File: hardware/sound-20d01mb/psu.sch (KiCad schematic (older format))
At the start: 3 parts

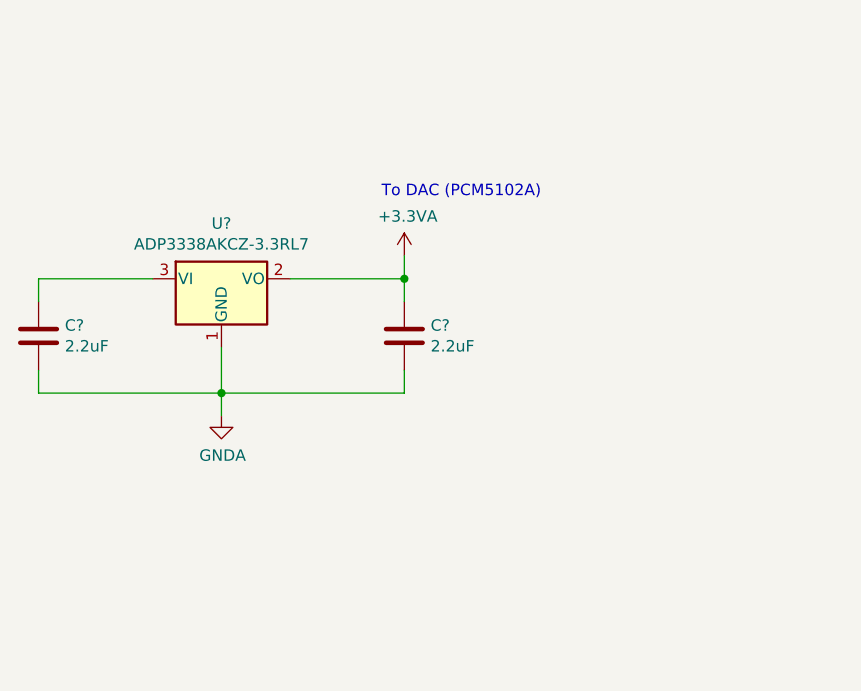
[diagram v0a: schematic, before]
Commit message: Updated power supply unit
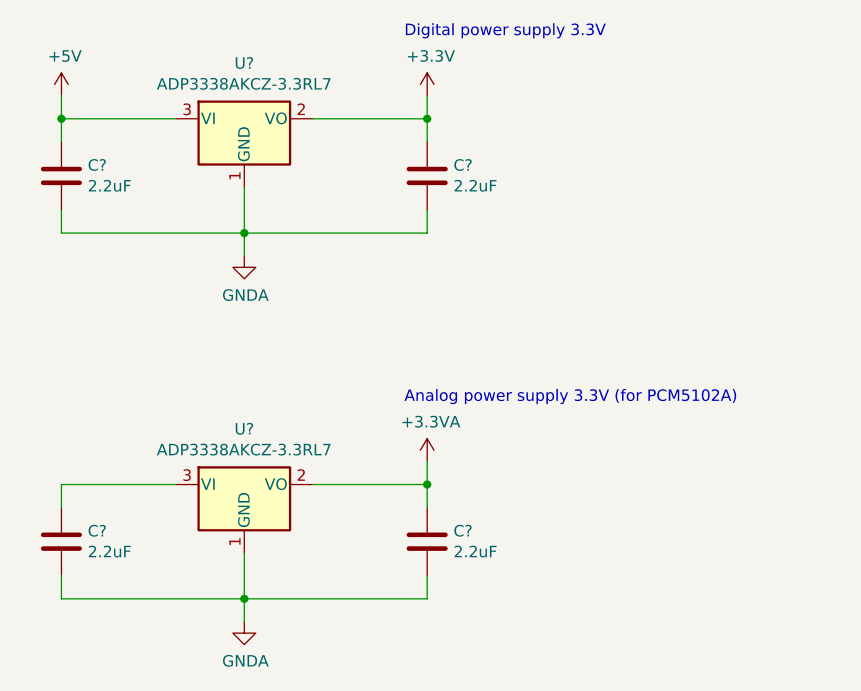
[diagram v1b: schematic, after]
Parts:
- added C? (x2): 2.2uF, Capacitor_SMD:C_1206_3216Metric_Pad1.42x1.75mm_HandSolder, symbol Device:C
- added U?: ADP3338AKCZ-3.3RL7, Package_TO_SOT_SMD:SOT-223-3_TabPin2, symbol Regulator_Linear:AZ1117-3.3
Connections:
- net GNDA: now also C?.2, C?.2, U?.1 (GND)
- new net +3V3: C?.1, U?.2 (VO)
- new net +5V: C?.1, U?.3 (VI)
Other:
- note added: "Analog power supply 3.3V (for PCM5102A)"
- note added: "Digital power supply 3.3V"
- note removed: "To DAC (PCM5102A)"
- moved on the sheet: C?, U?
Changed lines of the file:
@@
 L Regulator_Linear:AZ1117-3.3 U?
 U 1 1 60DF628F
-P 4350 3150
-F 0 "U?" H 4350 3392 50  0000 C CNN
-F 1 "ADP3338AKCZ-3.3RL7" H 4350 3301 50  0000 C CNN
-F 2 "Package_TO_SOT_SMD:SOT-223-3_TabPin2" H 4350 3400 50  0001 C CIN
-F 3 "https://www.analog.com/media/en/technical-documentation/data-sheets/adp3338.pdf" H 4350 3150 50  0001 C CNN
-	1    4350 3150
+P 4450 4050
+F 0 "U?" H 4450 4292 50  0000 C CNN
+F 1 "ADP3338AKCZ-3.3RL7" H 4450 4201 50  0000 C CNN
+F 2 "Package_TO_SOT_SMD:SOT-223-3_TabPin2" H 4450 4300 50  0001 C CIN
+F 3 "https://www.analog.com/media/en/technical-documentation/data-sheets/adp3338.pdf" H 4450 4050 50  0001 C CNN
+	1    4450 4050
 	1    0    0    -1
 $EndComp
@@
 L Device:C C?
 U 1 1 60E015B2
-P 5150 3400
+P 5250 4300
 AR Path="/60DE2DF4/60E015B2" Ref="C?"  Part="1"
 AR Path="/60DE2DF1/60E015B2" Ref="C?"  Part="1"
 AR Path="/61033008/60E015B2" Ref="C?"  Part="1"
-F 0 "C?" H 5265 3446 50  0000 L CNN
-F 1 "2.2uF" H 5265 3355 50  0000 L CNN
-F 2 "Capacitor_SMD:C_1206_3216Metric_Pad1.42x1.75mm_HandSolder" H 5188 3250 50  0001 C CNN
-F 3 "~" H 5150 3400 50  0001 C CNN
-	1    5150 3400
+F 0 "C?" H 5365 4346 50  0000 L CNN
+F 1 "2.2uF" H 5365 4255 50  0000 L CNN
+F 2 "Capacitor_SMD:C_1206_3216Metric_Pad1.42x1.75mm_HandSolder" H 5288 4150 50  0001 C CNN
+F 3 "~" H 5250 4300 50  0001 C CNN
+	1    5250 4300
 	1    0    0    -1
 $EndComp
@@
 L Device:C C?
 U 1 1 60E01602
-P 3550 3400
+P 3650 4300
 AR Path="/60DE2DF4/60E01602" Ref="C?"  Part="1"
 AR Path="/60DE2DF1/60E01602" Ref="C?"  Part="1"
 AR Path="/61033008/60E01602" Ref="C?"  Part="1"
-F 0 "C?" H 3665 3446 50  0000 L CNN
-F 1 "2.2uF" H 3665 3355 50  0000 L CNN
-F 2 "Capacitor_SMD:C_1206_3216Metric_Pad1.42x1.75mm_HandSolder" H 3588 3250 50  0001 C CNN
-F 3 "~" H 3550 3400 50  0001 C CNN
-	1    3550 3400
+F 0 "C?" H 3765 4346 50  0000 L CNN
+F 1 "2.2uF" H 3765 4255 50  0000 L CNN
+F 2 "Capacitor_SMD:C_1206_3216Metric_Pad1.42x1.75mm_HandSolder" H 3688 4150 50  0001 C CNN
+F 3 "~" H 3650 4300 50  0001 C CNN
+	1    3650 4300
 	1    0    0    -1
 $EndComp
@@
 L power:GNDA #PWR?
 U 1 1 60E01644
-P 4350 3750
-F 0 "#PWR?" H 4350 3500 50  0001 C CNN
-F 1 "GNDA" H 4355 3577 50  0000 C CNN
-F 2 "" H 4350 3750 50  0001 C CNN
-F 3 "" H 4350 3750 50  0001 C CNN
-	1    4350 3750
+P 4450 4650
+F 0 "#PWR?" H 4450 4400 50  0001 C CNN
+F 1 "GNDA" H 4455 4477 50  0000 C CNN
+F 2 "" H 4450 4650 50  0001 C CNN
+F 3 "" H 4450 4650 50  0001 C CNN
+	1    4450 4650
 	1    0    0    -1
 $EndComp
 Wire Wire Line
-	4350 3450 4350 3650
+	4450 4350 4450 4550
 $Comp
 L power:+3.3VA #PWR?
 U 1 1 60E017A8
-P 5150 3050
-F 0 "#PWR?" H 5150 2900 50  0001 C CNN
-F 1 "+3.3VA" H 5165 3223 50  0000 C CNN
-F 2 "" H 5150 3050 50  0001 C CNN
-F 3 "" H 5150 3050 50  0001 C CNN
-	1    5150 3050
+P 5250 3950
+F 0 "#PWR?" H 5250 3800 50  0001 C CNN
+F 1 "+3.3VA" H 5265 4123 50  0000 C CNN
+F 2 "" H 5250 3950 50  0001 C CNN
+F 3 "" H 5250 3950 50  0001 C CNN
+	1    5250 3950
 	1    0    0    -1
 $EndComp
 Wire Wire Line
-	4650 3150 5150 3150
+	4750 4050 5250 4050
 Wire Wire Line
-	5150 3150 5150 3050
+	5250 4050 5250 3950
 Wire Wire Line
-	5150 3150 5150 3250
-Connection ~ 5150 3150
+	5250 4050 5250 4150
+Connection ~ 5250 4050
 Wire Wire Line
-	5150 3550 5150 3650
+	5250 4450 5250 4550
 Wire Wire Line
-	5150 3650 4350 3650
+	5250 4550 4450 4550
 Wire Wire Line
-	4350 3650 4350 3750
-Connection ~ 4350 3650
+	4450 4550 4450 4650
+Connection ~ 4450 4550
 Wire Wire Line
-	3550 3150 4050 3150
+	3650 4050 4150 4050
 Wire Wire Line
-	4350 3650 3550 3650
+	4450 4550 3650 4550
 Wire Wire Line
-	3550 3650 3550 3550
+	3650 4550 3650 4450
 Wire Wire Line
-	3550 3150 3550 3250
-Text Notes 5050 2800 0    50   ~ 0
-To DAC (PCM5102A)
+	3650 4050 3650 4150
+Text Notes 5150 3700 0    50   ~ 0
+Analog power supply 3.3V (for PCM5102A)
+$Comp
+L Regulator_Linear:AZ1117-3.3 U?
+U 1 1 60E0E9BB
+P 4450 2450
+F 0 "U?" H 4450 2692 50  0000 C CNN
+F 1 "ADP3338AKCZ-3.3RL7" H 4450 2601 50  0000 C CNN
+F 2 "Package_TO_SOT_SMD:SOT-223-3_TabPin2" H 4450 2700 50  0001 C CIN
+F 3 "https://www.analog.com/media/en/technical-documentation/data-sheets/adp3338.pdf" H 4450 2450 50  0001 C CNN
+	1    4450 2450
+	1    0    0    -1
+$EndComp
+$Comp
+L Device:C C?
+U 1 1 60E0E9C1
+P 5250 2700
+AR Path="/60DE2DF4/60E0E9C1" Ref="C?"  Part="1"
+AR Path="/60DE2DF1/60E0E9C1" Ref="C?"  Part="1"
+AR Path="/61033008/60E0E9C1" Ref="C?"  Part="1"
+F 0 "C?" H 5365 2746 50  0000 L CNN
+F 1 "2.2uF" H 5365 2655 50  0000 L CNN
+F 2 "Capacitor_SMD:C_1206_3216Metric_Pad1.42x1.75mm_HandSolder" H 5288 2550 50  0001 C CNN
+F 3 "~" H 5250 2700 50  0001 C CNN
+	1    5250 2700
+	1    0    0    -1
+$EndComp
+$Comp
+L Device:C C?
+U 1 1 60E0E9C7
+P 3650 2700
+AR Path="/60DE2DF4/60E0E9C7" Ref="C?"  Part="1"
+AR Path="/60DE2DF1/60E0E9C7" Ref="C?"  Part="1"
+AR Path="/61033008/60E0E9C7" Ref="C?"  Part="1"
+F 0 "C?" H 3765 2746 50  0000 L CNN
+F 1 "2.2uF" H 3765 2655 50  0000 L CNN
+F 2 "Capacitor_SMD:C_1206_3216Metric_Pad1.42x1.75mm_HandSolder" H 3688 2550 50  0001 C CNN
+F 3 "~" H 3650 2700 50  0001 C CNN
+	1    3650 2700
+	1    0    0    -1
+$EndComp
+$Comp
+L power:GNDA #PWR?
+U 1 1 60E0E9CD
+P 4450 3050
+F 0 "#PWR?" H 4450 2800 50  0001 C CNN
+F 1 "GNDA" H 4455 2877 50  0000 C CNN
+F 2 "" H 4450 3050 50  0001 C CNN
+F 3 "" H 4450 3050 50  0001 C CNN
+	1    4450 3050
+	1    0    0    -1
+$EndComp
+Wire Wire Line
+	4450 2750 4450 2950
+Wire Wire Line
+	4750 2450 5250 2450
+Wire Wire Line
+	5250 2450 5250 2350
+Wire Wire Line
+	5250 2450 5250 2550
+Connection ~ 5250 2450
+Wire Wire Line
+	5250 2850 5250 2950
+Wire Wire Line
+	5250 2950 4450 2950
+Wire Wire Line
+	4450 2950 4450 3050
+Connection ~ 4450 2950
+Wire Wire Line
+	3650 2450 4150 2450
+Wire Wire Line
+	4450 2950 3650 2950
+Wire Wire Line
+	3650 2950 3650 2850
+Wire Wire Line
+	3650 2450 3650 2550
+$Comp
+L power:+3.3V #PWR?
+U 1 1 60E0F338
+P 5250 2350
+F 0 "#PWR?" H 5250 2200 50  0001 C CNN
+F 1 "+3.3V" H 5265 2523 50  0000 C CNN
+F 2 "" H 5250 2350 50  0001 C CNN
+F 3 "" H 5250 2350 50  0001 C CNN
+	1    5250 2350
+	1    0    0    -1
+$EndComp
+$Comp
+L power:+5V #PWR?
+U 1 1 60E0F3AB
+P 3650 2350
+F 0 "#PWR?" H 3650 2200 50  0001 C CNN
+F 1 "+5V" H 3665 2523 50  0000 C CNN
+F 2 "" H 3650 2350 50  0001 C CNN
+F 3 "" H 3650 2350 50  0001 C CNN
+	1    3650 2350
+	1    0    0    -1
+$EndComp
+Wire Wire Line
+	3650 2350 3650 2450
+Connection ~ 3650 2450
+Text Notes 5150 2100 0    50   ~ 0
+Digital power supply 3.3V
 $EndSCHEMATC

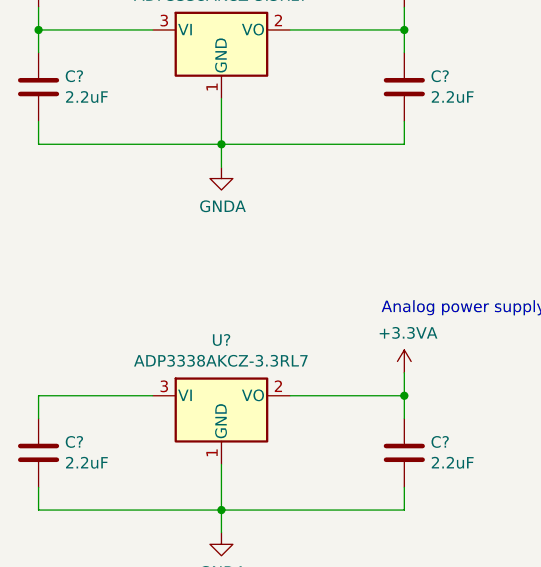
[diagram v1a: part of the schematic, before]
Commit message: Added Gain Settings
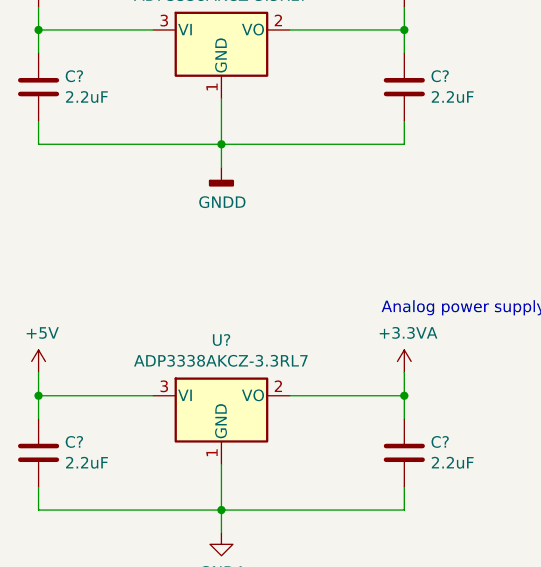
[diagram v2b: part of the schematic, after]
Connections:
- net +5V: now also C?.1, U?.3 (VI)
- net GNDA: no longer C?.2, C?.2, U?.1 (GND)
- new net GNDD: C?.2, C?.2, U?.1 (GND)
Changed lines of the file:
@@
-	1    0    0    -1
-$EndComp
-$Comp
-L power:GNDA #PWR?
-U 1 1 60E0E9CD
-P 4450 3050
-F 0 "#PWR?" H 4450 2800 50  0001 C CNN
-F 1 "GNDA" H 4455 2877 50  0000 C CNN
-F 2 "" H 4450 3050 50  0001 C CNN
-F 3 "" H 4450 3050 50  0001 C CNN
-	1    4450 3050
 	1    0    0    -1
 $EndComp
@@
 Text Notes 5150 2100 0    50   ~ 0
 Digital power supply 3.3V
+$Comp
+L power:GNDD #PWR?
+U 1 1 60E17887
+P 4450 3050
+F 0 "#PWR?" H 4450 2800 50  0001 C CNN
+F 1 "GNDD" H 4454 2895 50  0000 C CNN
+F 2 "" H 4450 3050 50  0001 C CNN
+F 3 "" H 4450 3050 50  0001 C CNN
+	1    4450 3050
+	1    0    0    -1
+$EndComp
+$Comp
+L power:+5V #PWR?
+U 1 1 60E17DB7
+P 3650 3950
+F 0 "#PWR?" H 3650 3800 50  0001 C CNN
+F 1 "+5V" H 3665 4123 50  0000 C CNN
+F 2 "" H 3650 3950 50  0001 C CNN
+F 3 "" H 3650 3950 50  0001 C CNN
+	1    3650 3950
+	1    0    0    -1
+$EndComp
+Wire Wire Line
+	3650 3950 3650 4050
+Connection ~ 3650 4050
 $EndSCHEMATC

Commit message: Updated PSU
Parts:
- added C?: 47uF, symbol Device:CP
- added C? (x2): 10uF, symbol Device:CP
- added C? (x2): 470uF, symbol Device:CP
- added C? (x2): 0.1uF, Capacitor_SMD:C_1206_3216Metric_Pad1.42x1.75mm_HandSolder, symbol Device:C
- added JP?: Jumper_3_Bridged12, Connector_PinHeader_2.54mm:PinHeader_1x03_P2.54mm_Vertical, symbol Jumper:Jumper_3_Bridged12
- added U?: L7805, symbol Regulator_Linear:L7805
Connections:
- net +3V3: now also C?.1
- net +5V: now also C?.1, C?.1, JP?.2 (C); no longer C?.1, U?.3 (VI)
- net GNDA: now also C?.2, C?.2, C?.2, C?.2, U?.2 (GND)
- net GNDD: now also C?.2, C?.2, C?.2
- new net: C?.1, C?.1, C?.1, U?.3 (OUT), U?.3 (VI)
- new net EXT_5V: JP?.3 (B)
- new net VBUS: JP?.1 (A)
- new net VCC: C?.1, C?.1, U?.1 (IN)
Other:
- note added: "Analog power supply +3.3VA (PCM5102A)"
- note added: "Digital power supply +3.3V"
- note added: "Place U? as close to the MCU as possible."
- note removed: "Analog power supply 3.3V (for PCM5102A)"
- note removed: "Digital power supply 3.3V"
- moved on the sheet: C?, U?

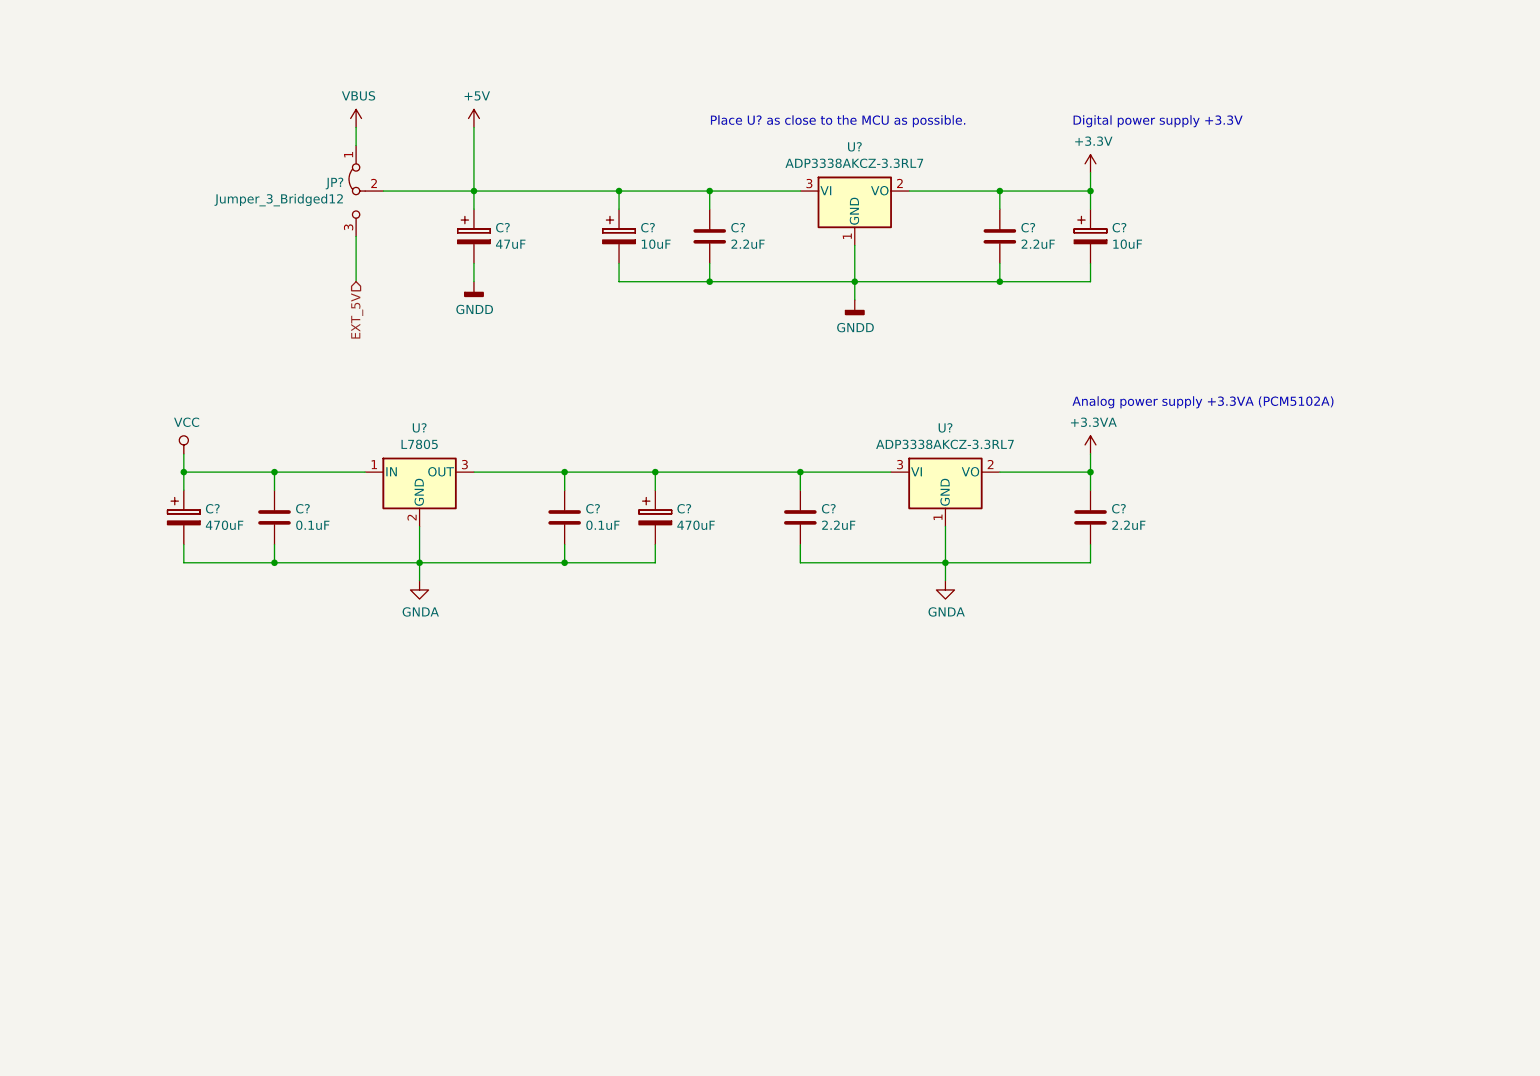
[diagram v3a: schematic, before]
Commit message: Added LM27762
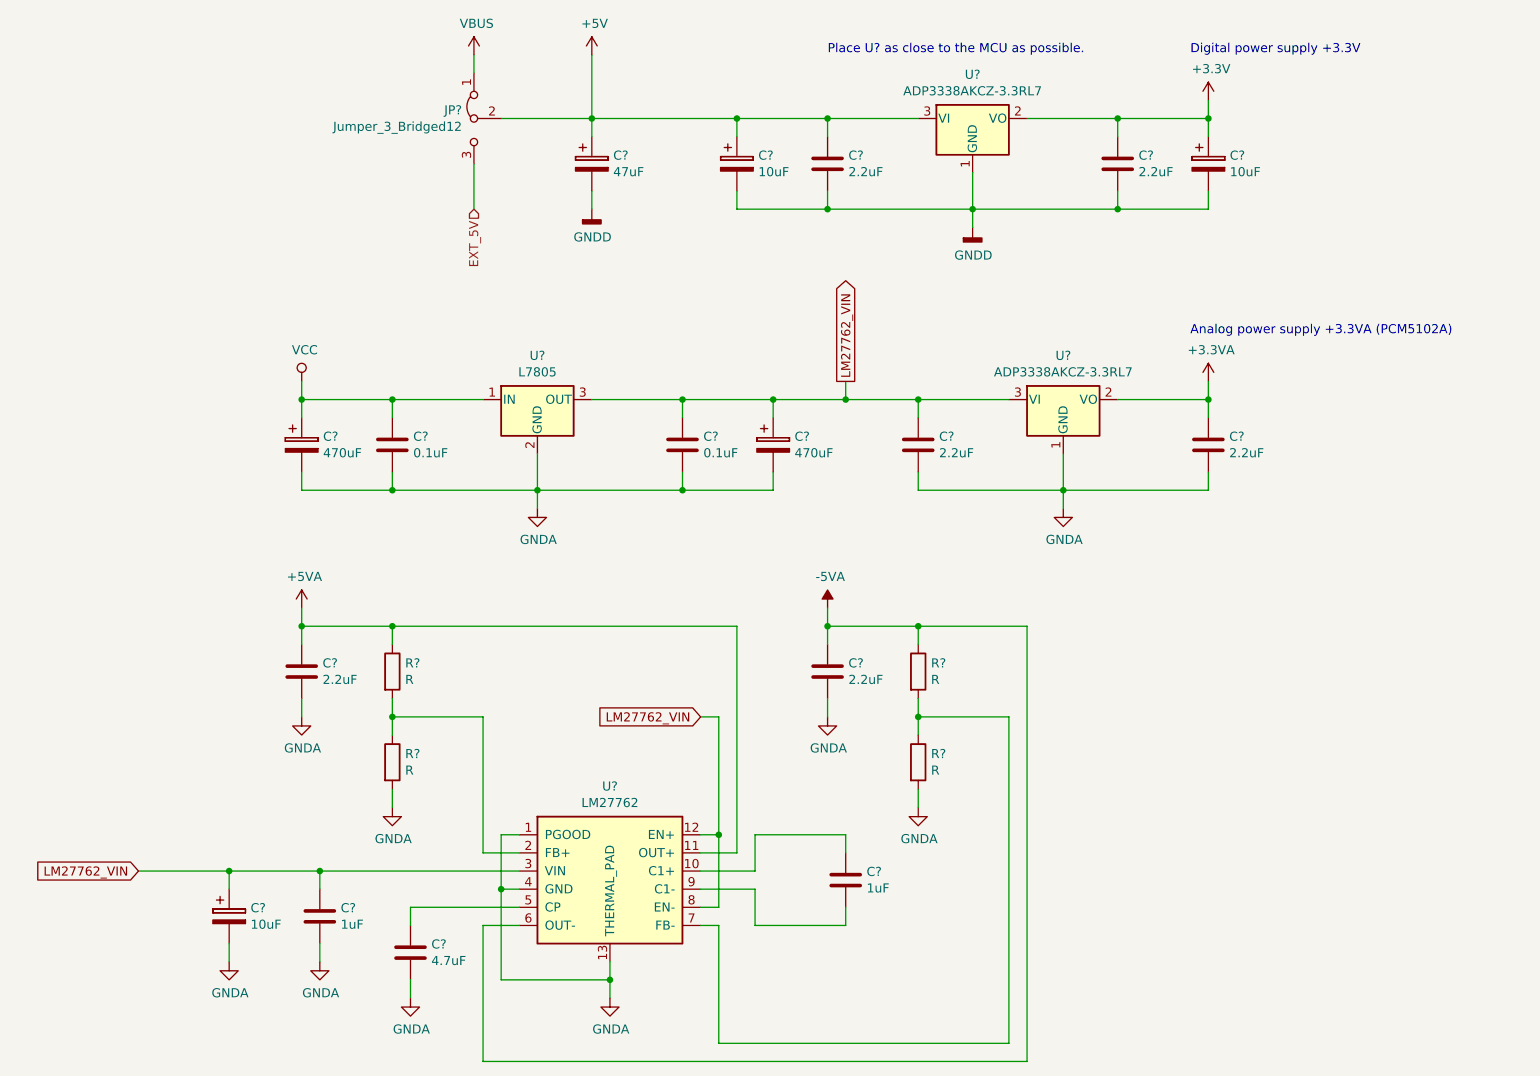
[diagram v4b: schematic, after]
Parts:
- added C?: 4.7uF, Capacitor_SMD:C_1206_3216Metric_Pad1.42x1.75mm_HandSolder, symbol Device:C
- added C? (x2): 1uF, Capacitor_SMD:C_1206_3216Metric_Pad1.42x1.75mm_HandSolder, symbol Device:C
- added C? (x2): 2.2uF, Capacitor_SMD:C_1206_3216Metric_Pad1.42x1.75mm_HandSolder, symbol Device:C
- added C?: 10uF, symbol Device:CP
- added R? (x4): R, Resistor_SMD:R_1206_3216Metric_Pad1.42x1.75mm_HandSolder, symbol Device:R
- added U?: LM27762, Package_SON:WSON-12-1EP_3x2mm_P0.5mm_EP1x2.65_ThermalVias, symbol sound-20d01_Library:LM27762
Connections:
- net GNDA: now also C?.2, C?.2, C?.2, C?.2, C?.2, R?.2, R?.2, U?.1 (PGOOD), U?.13 (THERMAL_PAD), U?.4 (GND)
- net LM27762_VIN: now reaches C?.1, C?.1, C?.1, U?.3 (OUT), U?.3 (VI)
- net LM27762_VIN: now also C?.1, C?.1, U?.12 (EN+), U?.3 (VIN), U?.8 (EN-)
- new net: C?.1, U?.10 (C1+)
- new net: R?.1, R?.2, U?.2 (FB+)
- new net: C?.1, U?.5 (CP)
- new net: R?.1, R?.2, U?.7 (FB-)
- new net: C?.2, U?.9 (C1-)
- new net +5VA: C?.1, R?.1, U?.11 (OUT+)
- new net -5VA: C?.1, R?.1, U?.6 (OUT-)
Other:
- moved on the sheet: C?, JP?, U?
